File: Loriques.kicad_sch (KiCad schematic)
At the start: 0 parts

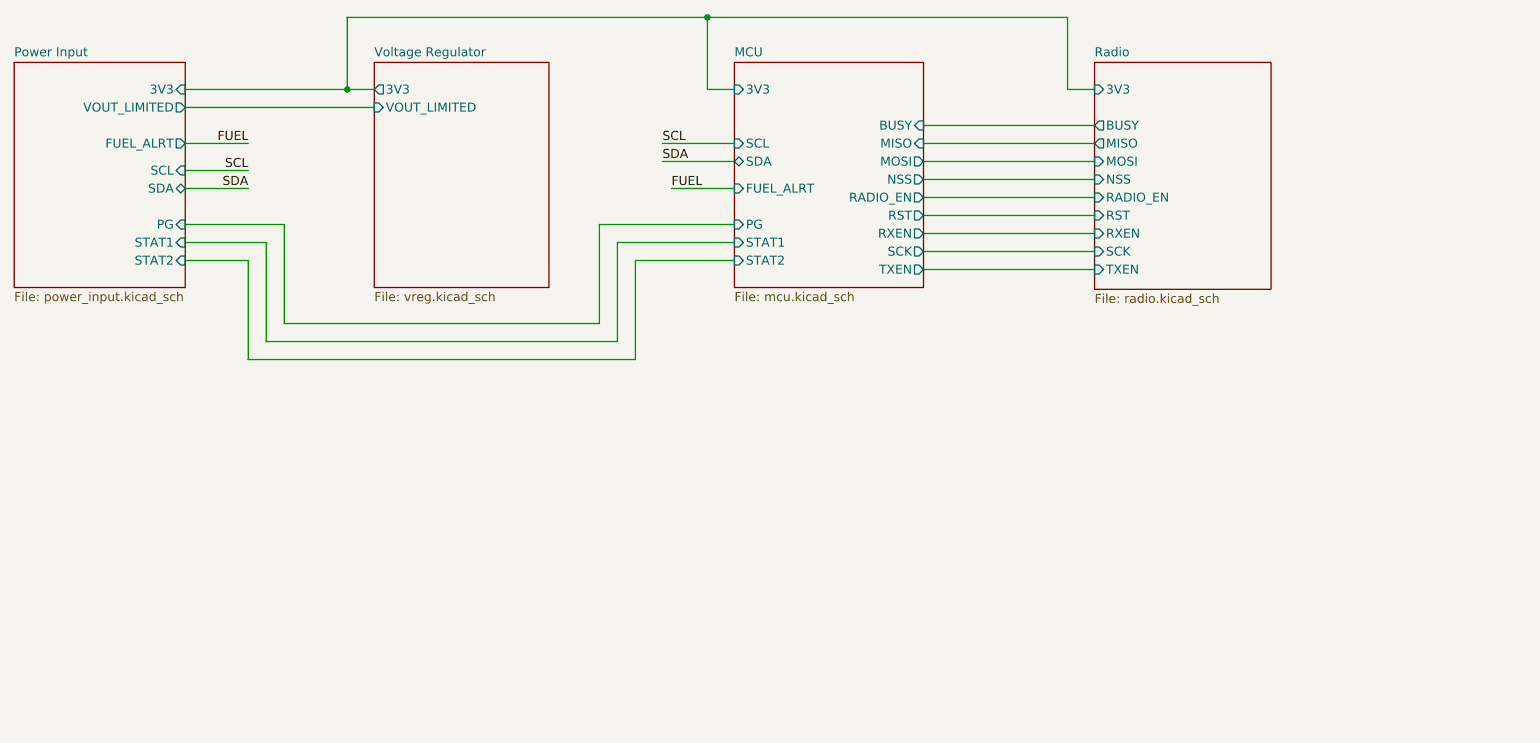
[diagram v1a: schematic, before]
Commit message: added logo to schematic sheets
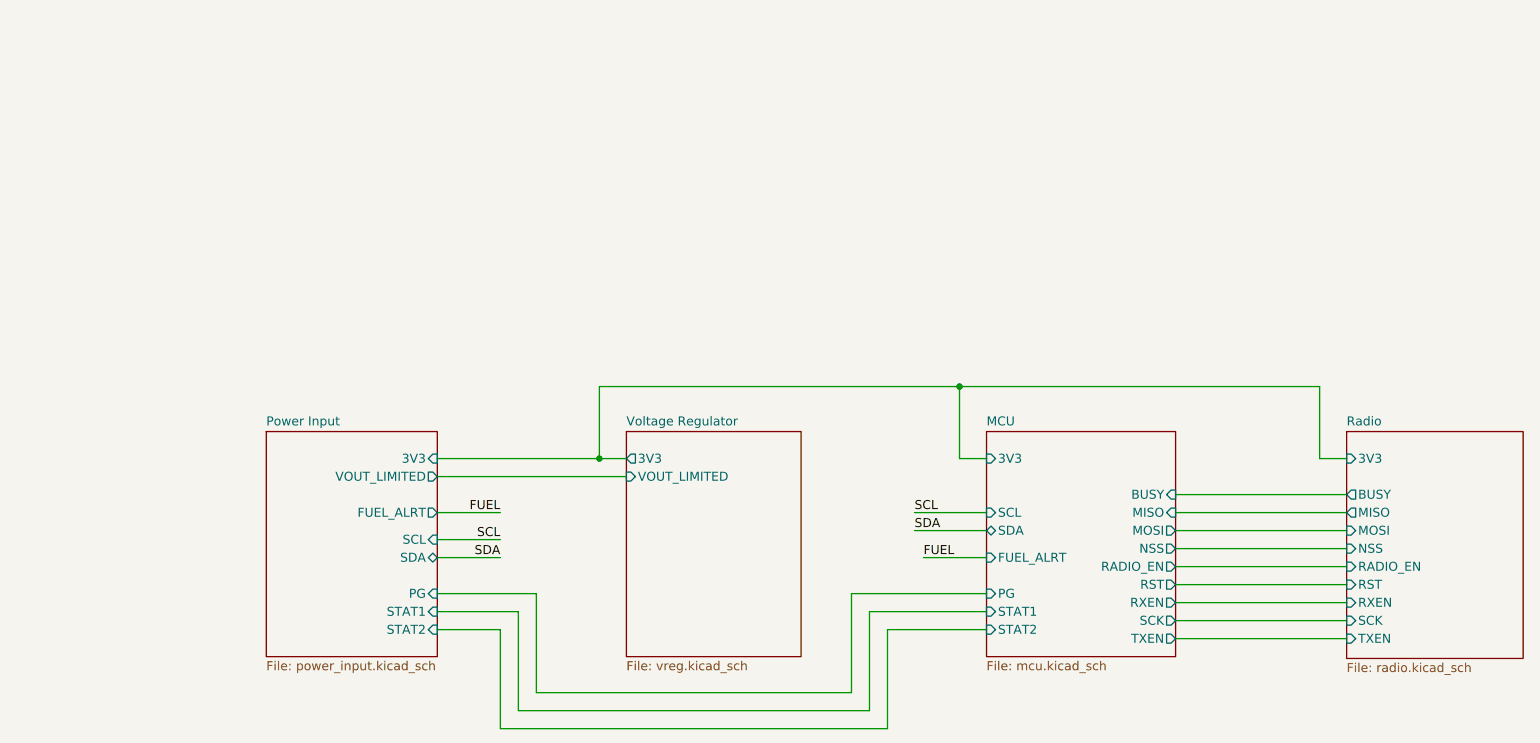
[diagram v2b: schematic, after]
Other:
- title: (none) -> Loriques
